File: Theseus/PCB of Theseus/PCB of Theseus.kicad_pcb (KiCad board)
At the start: 2 copper layers, 125 x 70 mm, 94 parts, among them J1 Screw_Terminal_01x04, J10 Screw_Terminal_01x03, J2 Screw_Terminal_01x04, J3 Screw_Terminal_01x03, J4 Screw_Terminal_01x06, J5 Programmer, J6 Micro_SD_Card, J7 Screw_Terminal_01x02, J8 Screw_Terminal_01x06, J9 Screw_Terminal_01x03, Q1 NMOS, Q2 NMOS, U1 TPS564257DRL, U10 INA326, U2 MCP2562, U3 REF200, U4 INA326, U5 INA326, U6 STM32H750VBTx, U7 REF200, U8 MX25L25645G, U9 REF200

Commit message: Theseus_Dev_Rev2
It's still the same PCB
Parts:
- removed H1, H2, H3, H4: ~, MountingHole:MountingHole_3.2mm_M3_Pad_Via
- removed J10, J9: Screw_Terminal_01x03, TerminalBlock_CUI:TerminalBlock_CUI_TB007-508-03_1x03_P5.08mm_Horizontal
- removed R10: 10k, Resistor_SMD:R_0402_1005Metric_Pad0.72x0.64mm_HandSolder
- removed R48, R49: 3.4k, Resistor_SMD:R_0402_1005Metric_Pad0.72x0.64mm_HandSolder
- removed R8: 221k, Resistor_SMD:R_0603_1608Metric_Pad0.98x0.95mm_HandSolder
- removed R9: 30k, Resistor_SMD:R_0603_1608Metric_Pad0.98x0.95mm_HandSolder
- removed U10, U5: INA326, Package_SO:MSOP-8_3x3mm_P0.65mm
- removed U7, U9: REF200, Package_SO:SOIC-8_3.9x4.9mm_P1.27mm
- added C25: 10u, Capacitor_SMD:C_0805_2012Metric_Pad1.18x1.45mm_HandSolder, F.Cu at (144.5, 86.1)
- added C26: 10u, Capacitor_SMD:C_0805_2012Metric_Pad1.18x1.45mm_HandSolder, B.Cu at (120.8, 79.4)
- added C27: 0.047u, Capacitor_SMD:C_0805_2012Metric_Pad1.18x1.45mm_HandSolder, F.Cu at (157.7, 78.1)
- added C28: 0.47u, Capacitor_SMD:C_0805_2012Metric_Pad1.18x1.45mm_HandSolder, F.Cu at (161.8, 78.1)
- added C29: 0.47u, Capacitor_SMD:C_0805_2012Metric_Pad1.18x1.45mm_HandSolder, F.Cu at (153.6, 78.1)
- added C30: 2n, Capacitor_SMD:C_0805_2012Metric_Pad1.18x1.45mm_HandSolder, F.Cu at (164.9, 62.3)
- added C31: 2n, Capacitor_SMD:C_0805_2012Metric_Pad1.18x1.45mm_HandSolder, F.Cu at (156.3, 62.3)
- added C32: 10u, Capacitor_SMD:C_0805_2012Metric_Pad1.18x1.45mm_HandSolder, F.Cu at (106.4, 54.5)
- added C33: 0.047u, Capacitor_SMD:C_0805_2012Metric_Pad1.18x1.45mm_HandSolder, F.Cu at (177.2, 80.8)
- added C34: 0.47u, Capacitor_SMD:C_0805_2012Metric_Pad1.18x1.45mm_HandSolder, F.Cu at (175.1, 77.2)
- added C35: 0.1u, Capacitor_SMD:C_0805_2012Metric_Pad1.18x1.45mm_HandSolder, F.Cu at (159.4, 40.1)
- added C36: 0.1u, Capacitor_SMD:C_0805_2012Metric_Pad1.18x1.45mm_HandSolder, F.Cu at (148.9, 66.6)
- added C37: 0.1u, Capacitor_SMD:C_0805_2012Metric_Pad1.18x1.45mm_HandSolder, F.Cu at (191.8, 84.8)
- added C38: 0.1u, Capacitor_SMD:C_0805_2012Metric_Pad1.18x1.45mm_HandSolder, F.Cu at (160.8, 65.2)
- added C39: 0.1u, Capacitor_SMD:C_0805_2012Metric_Pad1.18x1.45mm_HandSolder, F.Cu at (178.3, 70.7)
- added FB1: FerriteBead, Resistor_SMD:R_0805_2012Metric_Pad1.20x1.40mm_HandSolder, F.Cu at (150.5, 49.6)
- added H5: MountingHole, MountingHole:MountingHole_4.3mm_M4, F.Cu at (93.3, 33.7)
- added H6: MountingHole, MountingHole:MountingHole_4.3mm_M4, F.Cu at (93.3, 93.7)
- added H7: MountingHole, MountingHole:MountingHole_4.3mm_M4, F.Cu at (208.3, 33.7)
- added H8: MountingHole, MountingHole:MountingHole_4.3mm_M4, F.Cu at (208.3, 93.7)
- added J11: TB002-500-02BE, TerminalBlock_CUI:TerminalBlock_CUI_TB007-508-02_1x02_P5.08mm_Horizontal, F.Cu at (154.6, 95.6)
- added J12: TB002-500-02BE, TerminalBlock_CUI:TerminalBlock_CUI_TB007-508-02_1x02_P5.08mm_Horizontal, F.Cu at (164.3, 31.2)
- added R29: 10M ±1%, Resistor_SMD:R_0805_2012Metric_Pad1.20x1.40mm_HandSolder, F.Cu at (160.6, 86.9)
- added R30: 1M ±0.1%, Resistor_SMD:R_0805_2012Metric_Pad1.20x1.40mm_HandSolder, F.Cu at (153.6, 87.1)
- added R31: 806R, Resistor_SMD:R_0805_2012Metric_Pad1.20x1.40mm_HandSolder, F.Cu at (159.5, 82.9)
- added R32: 806R, Resistor_SMD:R_0805_2012Metric_Pad1.20x1.40mm_HandSolder, F.Cu at (155.7, 82.9)
- added R33: 20k, Resistor_SMD:R_0805_2012Metric_Pad1.20x1.40mm_HandSolder, F.Cu at (158.7, 71.2)
- added R34: 80.6k, Resistor_SMD:R_0805_2012Metric_Pad1.20x1.40mm_HandSolder, F.Cu at (165.0, 65.8)
- added R35: 20k, Resistor_SMD:R_0805_2012Metric_Pad1.20x1.40mm_HandSolder, F.Cu at (150.1, 71.0)
- added R36: 80.6k, Resistor_SMD:R_0805_2012Metric_Pad1.20x1.40mm_HandSolder, F.Cu at (156.3, 65.9)
- added R37: 806R, Resistor_SMD:R_0805_2012Metric_Pad1.20x1.40mm_HandSolder, F.Cu at (177.1, 84.1)
- added R38: 8.06k, Resistor_SMD:R_0805_2012Metric_Pad1.20x1.40mm_HandSolder, F.Cu at (179.5, 75.4)
- added TH1: PTS060301B100RP100, Resistor_SMD:R_0603_1608Metric_Pad0.98x0.95mm_HandSolder, F.Cu at (188.2, 99.1)
- added TP10: TestPoint, TestPoint:TestPoint_Pad_D2.0mm, F.Cu at (91.0, 61.6)
- added TP2: TC2+, TestPoint:TestPoint_Pad_D2.0mm, F.Cu at (163.2, 83.0)
- added TP3: TC2-, TestPoint:TestPoint_Pad_D2.0mm, F.Cu at (151.9, 83.0)
- added TP4: TC1+, TestPoint:TestPoint_Pad_D2.0mm, F.Cu at (175.3, 31.5)
- added TP5: TC1-, TestPoint:TestPoint_Pad_D2.0mm, F.Cu at (158.8, 31.3)
- added TP6: TC3+, TestPoint:TestPoint_Pad_D2.0mm, F.Cu at (188.1, 85.9)
- added TP7: TC3-, TestPoint:TestPoint_Pad_D2.0mm, F.Cu at (173.1, 85.8)
- added TP8: RTD1, TestPoint:TestPoint_Pad_D2.0mm, F.Cu at (193.1, 98.1)
- added TP9: RTD2, TestPoint:TestPoint_Pad_D2.0mm, F.Cu at (196.9, 98.1)
- added U11: INA326, Package_SO:MSOP-8_3x3mm_P0.65mm, F.Cu at (163.0, 71.0)
- added U12: INA326, Package_SO:MSOP-8_3x3mm_P0.65mm, F.Cu at (154.3, 71.1)
- added U13: MAX6675, Package_SO:SOIC-8_3.9x4.9mm_P1.27mm, F.Cu at (166.8, 42.6)
- C1: value 100nF -> 10u; footprint Capacitor_SMD:C_0603_1608Metric_Pad1.08x0.95mm_HandSolder -> Capacitor_SMD:C_0805_2012Metric_Pad1.18x1.45mm_HandSolder
- C10, C11, C12, C13, C14, C15, C16, C22, C6, C7, C9: footprint Capacitor_SMD:C_0603_1608Metric_Pad1.08x0.95mm_HandSolder -> Capacitor_SMD:C_0805_2012Metric_Pad1.18x1.45mm_HandSolder
- C17: value 1u -> 1n; footprint Capacitor_SMD:C_0402_1005Metric_Pad0.74x0.62mm_HandSolder -> Capacitor_SMD:C_0805_2012Metric_Pad1.18x1.45mm_HandSolder
- C18, C19: value 0.1uF -> 0.1u; footprint Capacitor_SMD:C_0201_0603Metric_Pad0.64x0.40mm_HandSolder -> Capacitor_SMD:C_0805_2012Metric_Pad1.18x1.45mm_HandSolder
- C2: value 22uF -> 100n
- C20, C21: value 510pF -> 0.5n; footprint Capacitor_SMD:C_0201_0603Metric_Pad0.64x0.40mm_HandSolder -> Capacitor_SMD:C_0805_2012Metric_Pad1.18x1.45mm_HandSolder
- C23: value 510pF -> 0.47u; footprint Capacitor_SMD:C_0201_0603Metric_Pad0.64x0.40mm_HandSolder -> Capacitor_SMD:C_0805_2012Metric_Pad1.18x1.45mm_HandSolder
- C24, C4: value 22uF -> 22u
- C3: value 10pF -> 100n; footprint Capacitor_SMD:C_0402_1005Metric_Pad0.74x0.62mm_HandSolder -> Capacitor_SMD:C_0805_2012Metric_Pad1.18x1.45mm_HandSolder
- C5: value 100nF -> 22u; footprint Capacitor_SMD:C_0603_1608Metric_Pad1.08x0.95mm_HandSolder -> Capacitor_SMD:C_0805_2012Metric_Pad1.18x1.45mm_HandSolder
- C8: footprint Capacitor_SMD:C_0603_1608Metric_Pad1.08x0.95mm_HandSolder -> Capacitor_SMD:C_0805_2012Metric_Pad1.18x1.45mm_HandSolder; moved to B.Cu
- D1, D5: value D -> 1N4150-W-E3-18; footprint Diode_SMD:D_SMB-SMC_Universal_Handsoldering -> Diode_SMD:D_SOD-123
- F1: value TBD -> 3.5A 0685T3500-01
- J1, J2: value Screw_Terminal_01x04 -> TB001-500-04BE
- J3: value Screw_Terminal_01x03 -> TB002-500-02BE; footprint TerminalBlock_CUI:TerminalBlock_CUI_TB007-508-03_1x03_P5.08mm_Horizontal -> TerminalBlock_CUI:TerminalBlock_CUI_TB007-508-02_1x02_P5.08mm_Horizontal
- J4, J8: value Screw_Terminal_01x06 -> TB003-500-P06BE
- J5: value Programmer -> Programmer GRPB022VWQS-RC
- J6: value Micro_SD_Card -> Micro SD Holder 0472192001
- J7: value Screw_Terminal_01x02 -> TB002-500-02BE
- L1: value 3.3uH -> 2.2u; footprint Fydp_footprints:VLS6045EX-3R3N -> Fydp_footprints:SPM6530T-2R2M
- Q1, Q2: value NMOS -> NX3020NAK,215
- R1, R2, R3: value 150R -> 150R ±0.1%; footprint Resistor_SMD:R_0603_1608Metric_Pad0.98x0.95mm_HandSolder -> Resistor_SMD:R_0805_2012Metric_Pad1.20x1.40mm_HandSolder
- R11: value 45.3k -> 33.2k; footprint Resistor_SMD:R_0603_1608Metric_Pad0.98x0.95mm_HandSolder -> Resistor_SMD:R_0805_2012Metric_Pad1.20x1.40mm_HandSolder
- R12: value 10k -> 10.2k; footprint Resistor_SMD:R_0402_1005Metric_Pad0.72x0.64mm_HandSolder -> Resistor_SMD:R_0805_2012Metric_Pad1.20x1.40mm_HandSolder
- R13, R14, R15, R16, R17: footprint Resistor_SMD:R_0402_1005Metric_Pad0.72x0.64mm_HandSolder -> Resistor_SMD:R_0805_2012Metric_Pad1.20x1.40mm_HandSolder; moved to B.Cu
- R18, R19: value 2k -> 32.4k ±0.1%; footprint Resistor_SMD:R_0603_1608Metric_Pad0.98x0.95mm_HandSolder -> Resistor_SMD:R_0805_2012Metric_Pad1.20x1.40mm_HandSolder
- R20: value 76.8R -> 100R ±0.1%; footprint Resistor_SMD:R_0603_1608Metric_Pad0.98x0.95mm_HandSolder -> Resistor_SMD:R_0805_2012Metric_Pad1.20x1.40mm_HandSolder
- R21: value 324k -> 8.06k; footprint Resistor_SMD:R_0201_0603Metric_Pad0.64x0.40mm_HandSolder -> Resistor_SMD:R_0805_2012Metric_Pad1.20x1.40mm_HandSolder
- R22: value 76.8R -> 200k; footprint Resistor_SMD:R_0603_1608Metric_Pad0.98x0.95mm_HandSolder -> Resistor_SMD:R_0805_2012Metric_Pad1.20x1.40mm_HandSolder
- R23: value 2k -> 200k; footprint Resistor_SMD:R_0603_1608Metric_Pad0.98x0.95mm_HandSolder -> Resistor_SMD:R_0805_2012Metric_Pad1.20x1.40mm_HandSolder
- R24, R25: value 324k -> 1M ±0.1%; footprint Resistor_SMD:R_0201_0603Metric_Pad0.64x0.40mm_HandSolder -> Resistor_SMD:R_0805_2012Metric_Pad1.20x1.40mm_HandSolder
- R26: value 76.8R -> 806R; footprint Resistor_SMD:R_0603_1608Metric_Pad0.98x0.95mm_HandSolder -> Resistor_SMD:R_0805_2012Metric_Pad1.20x1.40mm_HandSolder
- R27, R28: footprint Resistor_SMD:R_0402_1005Metric_Pad0.72x0.64mm_HandSolder -> Resistor_SMD:R_0805_2012Metric_Pad1.20x1.40mm_HandSolder
- R4, R44, R45, R5, R6, R7: footprint Resistor_SMD:R_0603_1608Metric_Pad0.98x0.95mm_HandSolder -> Resistor_SMD:R_0805_2012Metric_Pad1.20x1.40mm_HandSolder
- R46: value 30K -> 3M ±1%; footprint Resistor_SMD:R_0603_1608Metric_Pad0.98x0.95mm_HandSolder -> Resistor_SMD:R_0805_2012Metric_Pad1.20x1.40mm_HandSolder
- R47: value 10K -> 1M ±0.1%; footprint Resistor_SMD:R_0402_1005Metric_Pad0.72x0.64mm_HandSolder -> Resistor_SMD:R_0805_2012Metric_Pad1.20x1.40mm_HandSolder
- U1: value TPS564257DRL -> TPS565201DDC; footprint Package_TO_SOT_SMD:SOT-563 -> Package_TO_SOT_SMD:SOT-23-6_Handsoldering
- U3: value REF200 -> INA326; footprint Package_SO:SOIC-8_3.9x4.9mm_P1.27mm -> Package_SO:MSOP-8_3x3mm_P0.65mm
- U8: footprint Package_SO:SOIC-16W_7.5x10.3mm_P1.27mm -> Package_SO:SOIC-8_5.3x5.3mm_P1.27mm
- moved D3 86.4 mm to (186.8, 50.1), turned to 180 degrees
- moved D4 85.8 mm to (198.2, 50.4), turned to 180 degrees
- moved R27 85.7 mm to (183.1, 42.1)
- moved R28 85.5 mm to (194.4, 42.0)
- moved D1 84.6 mm to (186.0, 40.0)
- moved Q1 84.4 mm to (186.8, 43.3), turned to -90 degrees
- moved D5 84.4 mm to (197.2, 39.8)
- moved Q2 84.2 mm to (198.1, 43.1), turned to -90 degrees
- moved R4 83.6 mm to (183.1, 50.1), turned to 0 degrees
- moved J1 83.2 mm to (182.7, 31.3)
- moved R7 83.1 mm to (194.4, 50.4), turned to 0 degrees
- moved C17 82.8 mm to (158.2, 49.5)
- moved C15 81.2 mm to (150.8, 44.5), turned to 0 degrees
- moved R6 81.0 mm to (181.1, 45.5), turned to 180 degrees
- moved R5 80.8 mm to (192.4, 45.5), turned to 180 degrees
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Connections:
- net /MCU/RTD_1 renamed /MCU/TC3
- C20 pad 1: Net-(U5-R2) -> Net-(U3-R2)
- C21 pad 2: GND -> Net-(C21-Pad2)
- C23 pad 1: Net-(U10-R2) -> GND
- C23 pad 2: GND -> Net-(U4-+)
- C3 pad 1: +3.3V -> Net-(U1-SW)
- C3 pad 2: Net-(U1-FB) -> Net-(U1-VBST)
- R11 pad 2: Net-(U1-FB) -> Net-(U1-VFB)
- R12 pad 1: Net-(U1-FB) -> Net-(U1-VFB)
- R18 pad 1: Net-(R18-Pad1) -> +3.3V
- R18 pad 2: Net-(R18-Pad2) -> /Temperature Sensors/RTD+
- R19 pad 1: Net-(R19-Pad1) -> +3.3V
- R19 pad 2: Net-(R19-Pad2) -> Net-(U3--)
- R20 pad 1: Net-(U5--) -> Net-(U3--)
- R20 pad 2: Net-(J10-Pin_1) -> GND
- R21 pad 1: Net-(U5-R2) -> Net-(R21-Pad1)
- R21 pad 2: GND -> Net-(R21-Pad2)
- R22 pad 1: Net-(U3-I2_LOW) -> Net-(U3-R2)
- R22 pad 2: Net-(J3-Pin_1) -> GND
- R23 pad 1: Net-(R23-Pad1) -> Net-(U4-R2)
- R23 pad 2: Net-(R23-Pad2) -> Net-(C21-Pad2)
- R24 pad 1: Net-(U4-R2) -> +3.3V
- R24 pad 2: GND -> Net-(J3-Pin_2)
- R25 pad 1: Net-(U10-R2) -> Net-(J3-Pin_1)
- R26 pad 1: Net-(U10--) -> Net-(J3-Pin_2)
- R26 pad 2: Net-(J9-Pin_1) -> Net-(U4-+)
- U1 pad 1: +BATT -> GND
- U1 pad 2: Net-(U1-EN) -> Net-(U1-SW)
- U1 pad 3: Net-(U1-SW) -> +BATT
- U1 pad 4: Net-(U1-PG) -> Net-(U1-VFB)
- U1 pad 5: Net-(U1-FB) -> +BATT
- U1 pad 6: GND -> Net-(U1-VBST)
- U3 pad 1: Net-(J3-Pin_2) -> Net-(R21-Pad1)
- U3 pad 2: Net-(U3-I2_LOW) -> Net-(U3--)
- U3 pad 3: unconnected-(U3-MIRROR_COMMON-Pad3) -> /Temperature Sensors/RTD+
- U3 pad 4: unconnected-(U3-MIRROR_OUTPUT-Pad4) -> GND
- U3 pad 5: unconnected-(U3-MIRROR_INPUT-Pad5) -> Net-(U3-R2)
- U3 pad 6: unconnected-(U3-SUBSTRATE-Pad6) -> Net-(C21-Pad2)
- U3 pad 8: +3.3V -> Net-(R21-Pad2)
- U4 pad 1: Net-(R19-Pad1) -> Net-(R38-Pad1)
- U4 pad 2: Net-(U3-I2_LOW) -> Net-(U4--)
- U4 pad 3: Net-(J3-Pin_2) -> Net-(U4-+)
- U4 pad 8: Net-(R19-Pad2) -> Net-(R38-Pad2)
- U6 pad 1: /MCU/RTD_3 -> /MCU/TC2+
- U6 pad 2: /MCU/RTD_2 -> /MCU/TC2-
- U6 pad 21: +3.3V -> Net-(U6-VDDA)
- U6 pad 28: /MCU/LED_BLUE -> /MCU/TC1_NSS
- U6 pad 29: /MCU/LED_RED -> /MCU/TC1_SCK
- U6 pad 33: unconnected-(U6-PC5-Pad33) -> /MCU/TC1_SI
- U6 pad 56: unconnected-(U6-PD9-Pad56) -> /MCU/LED_RED
- U6 pad 57: unconnected-(U6-PD10-Pad57) -> /MCU/LED_BLUE
- U8 pad 1: unconnected-(U8-NC/SOIC3-Pad1) -> /MCU/SPI_NSS
- U8 pad 2: +3.3V -> /MCU/SPI_MISO
- U8 pad 3: /MCU/MEM_~{RESET} -> unconnected-(U8-WP#/SIO2-Pad3)
- U8 pad 4: unconnected-(U8-NC-Pad4) -> GND
- U8 pad 5: unconnected-(U8-NC-Pad5) -> /MCU/SPI_MOSI
- U8 pad 6: unconnected-(U8-NC-Pad6) -> /MCU/SPI_SCK
- U8 pad 7: /MCU/SPI_NSS -> /MCU/MEM_~{RESET}
- U8 pad 8: /MCU/SPI_MISO -> +3.3V
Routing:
- net GND: track 141.8 -> 208.8 mm, vias 5 -> 23
- net +3.3V: track 85.2 -> 137.4 mm
- net +BATT: track 96.0 -> 146.3 mm
- net /MCU/RTD_2: track 40.1 -> 0.00 mm
- net /CAN_Rx: track 66.2 -> 27.1 mm
- net /MCU/VALVE_2: track 23.6 -> 60.7 mm
- net /CAN_Tx: track 58.6 -> 22.6 mm
- net /MCU/VALVE_1: track 13.2 -> 44.6 mm
- net /MCU/SD_CLK: track 58.5 -> 28.9 mm
- net /MCU/TC1_SI: track 0.00 -> 29.3 mm
- net /MCU/SD_D0: track 75.2 -> 47.3 mm, vias 0 -> 1
- net /MCU/SPI_MISO: track 36.7 -> 9.02 mm
- net /MCU/PT_1: track 50.3 -> 22.9 mm
- net /MCU/TC1_NSS: track 0.00 -> 25.6 mm
- net /MCU/PT_2: track 40.5 -> 15.3 mm
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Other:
- board size 125 x 70 mm -> 135 x 80 mm
- board text added: "BATT"
- board text added: "CAN"
- board text added: "HALL"
- board text added: "MATTHEW GORDON"
- board text added: "PCB OF THESEUS DEV EDITION, REV 2"
- board text added: "PT"
- board text added: "TC1"
- board text added: "TC2"
- board text added: "TC3"
- board text removed: "+12V"
- board text removed: "+3.3V"
- board text removed: "5V"
- board text removed: "CANH"
- board text removed: "CANL"
- board text removed: "GND"
- board text removed: "HALL SENSORS"
- board text removed: "IF YOU'RE READING THIS, YOU'RE HOLDING THE PCB UPSIDE DOWN"
- board text removed: "PTS"
- board text removed: "RTD"
- board text removed: "SENSE"
- board text removed: "THE PCB OF THESEUS REV. 1.0 MATTHEW GORDON"

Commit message: Minor routing changes
Still the same PCB
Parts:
- added G***: LOGO, Tutorial_Footprints:Logo_Horizontal_Silkscreen_10mm, B.Cu at (147.3, 66.4)
- moved C13 23.0 mm to (158.9, 52.9), turned to 0 degrees
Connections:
- U6 pad 30: unconnected-(U6-PA6-Pad30) -> /MCU/TC1_SI
- U6 pad 33: /MCU/TC1_SI -> unconnected-(U6-PC5-Pad33)
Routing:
- net +3.3V: track 137.4 -> 140.0 mm
- net /MCU/TC1_SI: track 29.3 -> 28.0 mm
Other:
- board text added: "IF YOU'RE READING THIS THE PCB IS UPSIDE-DOWN (OR YOU'RE IN THE SHADOW REALM)"

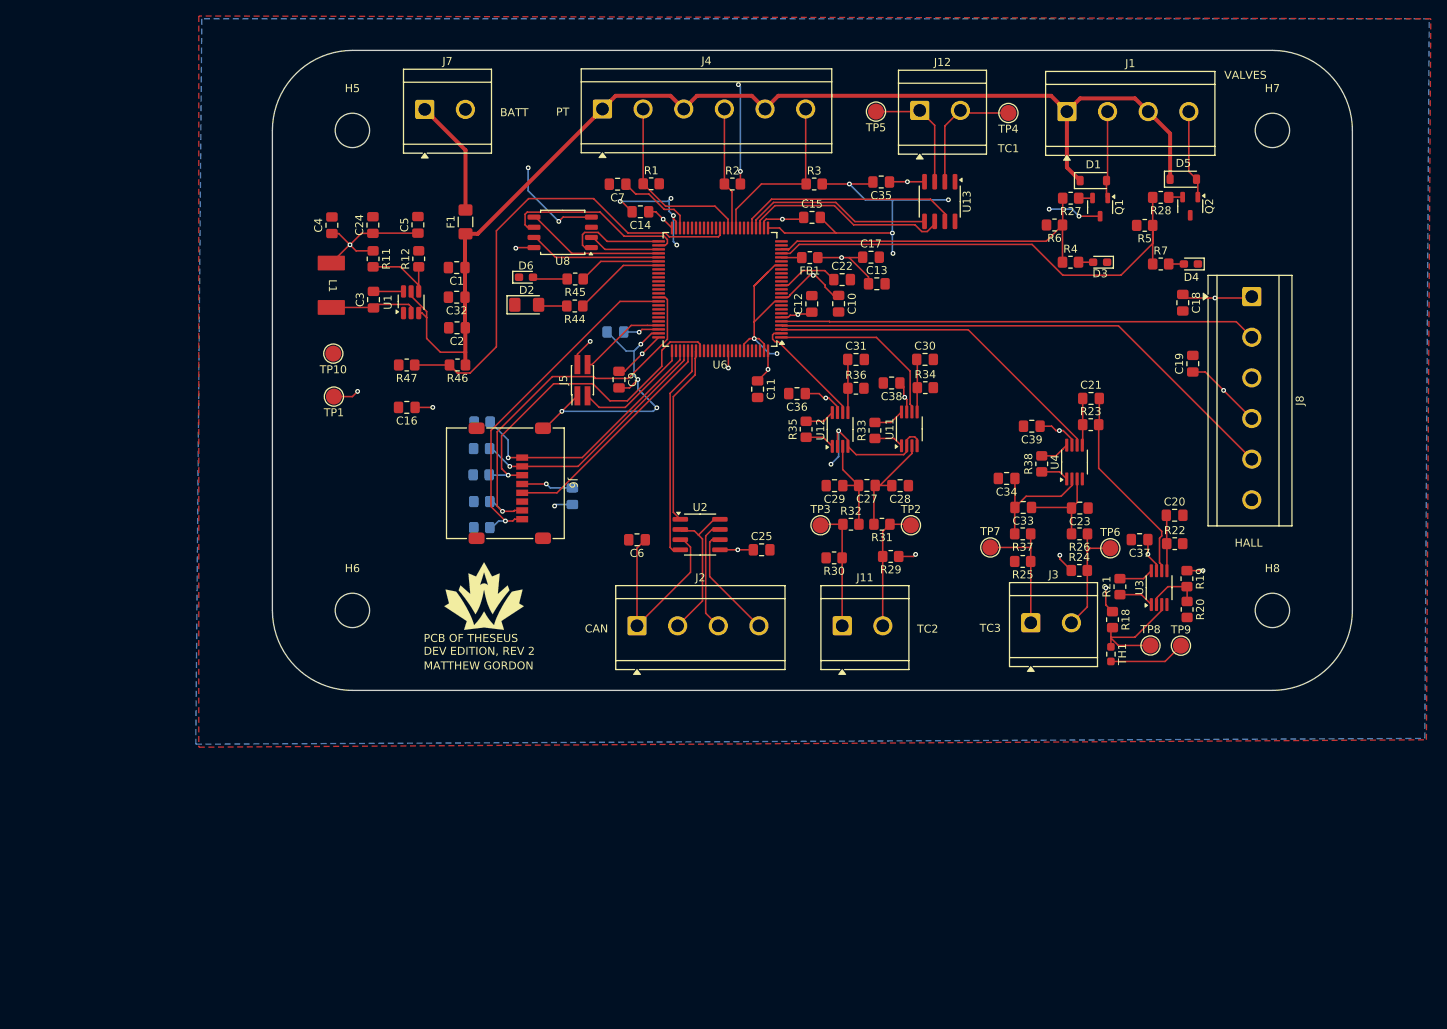
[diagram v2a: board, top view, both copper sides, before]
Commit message: Fixes V3
- Copied Ferrite Bead P/N from processor
- Added external oscillator
- Made status LED pins pull-down
- Copied processor programming header
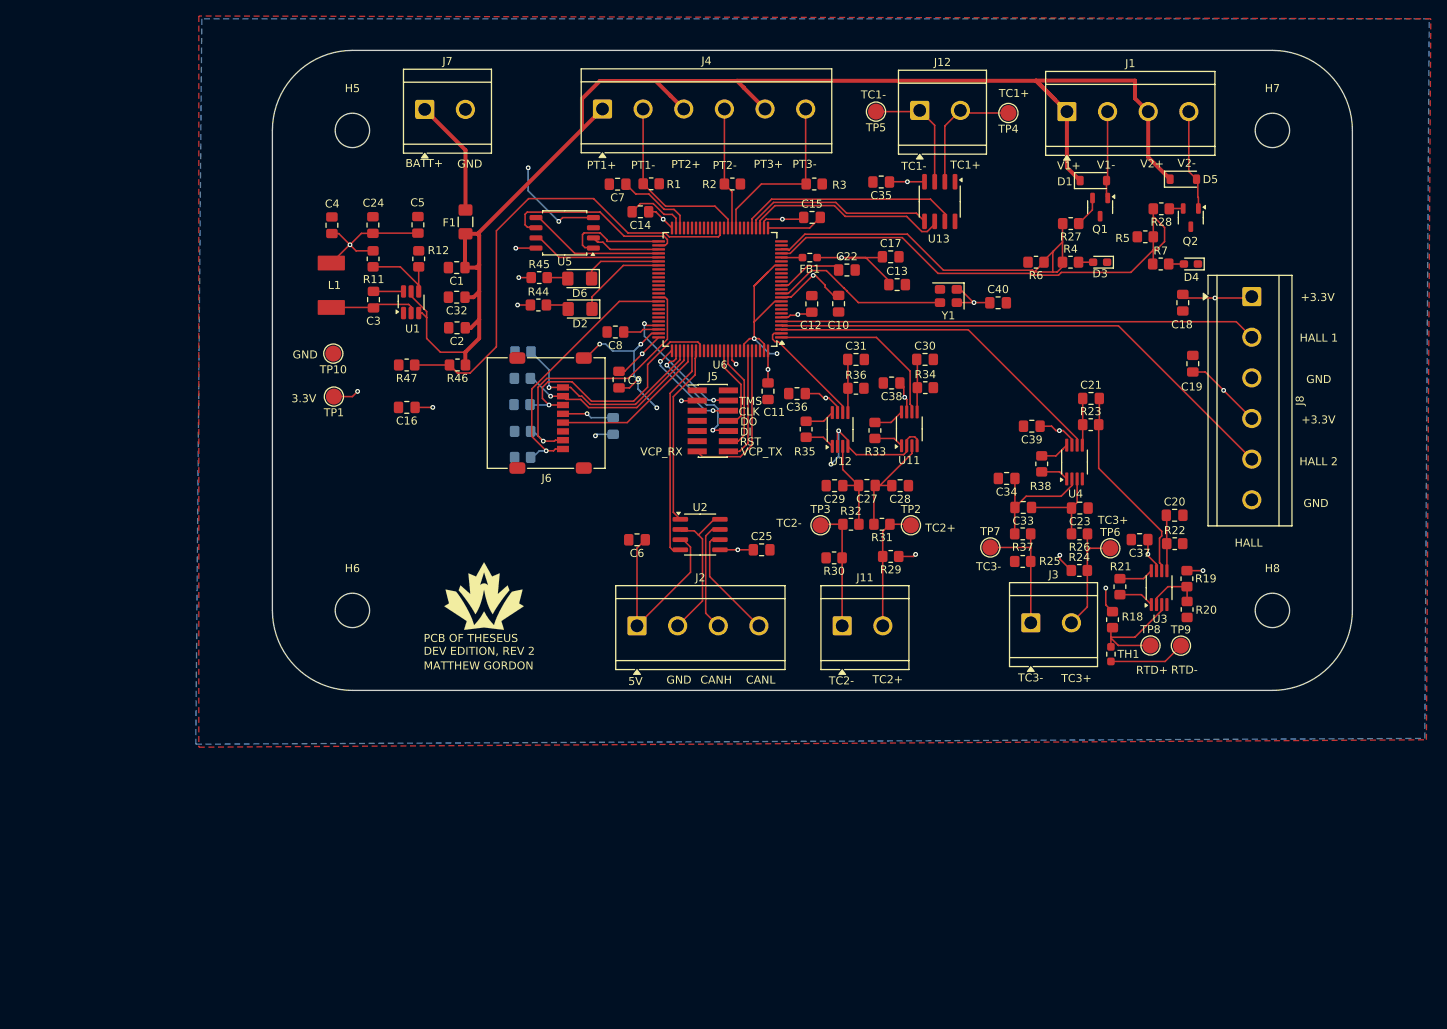
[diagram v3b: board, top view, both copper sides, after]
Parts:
- removed U8: MX25L25645G, Package_SO:SOIC-8_5.3x5.3mm_P1.27mm
- added C40: 0.01uF, Capacitor_SMD:C_0805_2012Metric_Pad1.18x1.45mm_HandSolder, F.Cu at (174.1, 55.2)
- added U5: MX25L25645G, Package_SO:SOIC-8_5.3x5.3mm_P1.27mm, F.Cu at (119.9, 46.5)
- added Y1: ASE-4.000MHz-L-C-T, Oscillator:Oscillator_SMD_Abracon_ASE-4Pin_3.2x2.5mm, F.Cu at (167.8, 54.4)
- C8: moved to F.Cu
- D6: footprint Diode_SMD:D_0603_1608Metric_Pad1.05x0.95mm_HandSolder -> Diode_SMD:D_1206_3216Metric_Pad1.42x1.75mm_HandSolder
- FB1: value FerriteBead -> PE-0603PFB121ST; footprint Resistor_SMD:R_0805_2012Metric_Pad1.20x1.40mm_HandSolder -> Resistor_SMD:R_0603_1608Metric_Pad0.98x0.95mm_HandSolder
- J5: value Programmer GRPB022VWQS-RC -> CN4 STDC14 (Programmer); footprint Connector_PinHeader_1.27mm:PinHeader_2x02_P1.27mm_Vertical_SMD -> Connector_PinHeader_1.27mm:PinHeader_2x07_P1.27mm_Vertical_SMD
- moved J5 17.1 mm to (138.4, 70.0), turned to 0 degrees
- moved C26 10.1 mm to (126.0, 70.6)
- moved J6 10.1 mm to (117.6, 69.0)
- moved R14 10.1 mm to (114.6, 64.7)
- moved R16 10.1 mm to (114.6, 71.3)
- moved R17 10.1 mm to (114.6, 74.5)
- moved R13 10.1 mm to (114.7, 61.4)
- moved R15 10.1 mm to (114.5, 68.0)
- moved D6 6.71 mm to (121.8, 52.2), turned to 180 degrees
- moved D2 6.70 mm to (121.8, 56.0), turned to 180 degrees
- moved R6 5.19 mm to (178.8, 50.1)
- moved R44 4.55 mm to (116.6, 55.5), turned to 0 degrees
- moved R45 4.50 mm to (116.7, 52.1), turned to 0 degrees
- moved R27 3.18 mm to (183.1, 45.3)
- moved C13 2.54 mm to (161.4, 53.0)
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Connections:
- net /MCU/SWDIO renamed /MCU/TMS
- D2 pad 1: GND -> /MCU/LED_BLUE
- D6 pad 1: GND -> /MCU/LED_RED
- J5 pad 1: GND -> unconnected-(J5-Pin_1-Pad1)
- J5 pad 2: +3.3V -> unconnected-(J5-Pin_2-Pad2)
- J5 pad 3: /MCU/SWCLK -> +3.3V
- R44 pad 1: /MCU/LED_BLUE -> +3.3V
- R45 pad 1: /MCU/LED_RED -> +3.3V
- U6 pad 12: unconnected-(U6-PH0-Pad12) -> /MCU/OSC_IN
- U6 pad 76: /MCU/SWCLK -> /MCU/TCK
- U6 pad 77: unconnected-(U6-PA15-Pad77) -> /MCU/TDI
- U6 pad 89: unconnected-(U6-PB3-Pad89) -> /MCU/TDO
- U6 pad 90: +3.3V -> /MCU/TRST
- U6 pad 91: unconnected-(U6-PB5-Pad91) -> +3.3V
- U6 pad 95: unconnected-(U6-PB8-Pad95) -> /MCU/VCP_TX
- U6 pad 96: unconnected-(U6-PB9-Pad96) -> /MCU/VCP_RX
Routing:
- net GND: track 208.8 -> 128.5 mm, vias 23 -> 11
- net +BATT: track 146.3 -> 180.9 mm
- net /MCU/OSC_IN: track 0.00 -> 22.7 mm
- net /MCU/VCP_RX: track 0.00 -> 19.5 mm
- net /MCU/TDI: track 0.00 -> 16.2 mm, vias 0 -> 2
- net /MCU/SWCLK: track 14.8 -> 0.00 mm
- net /MCU/VCP_TX: track 0.00 -> 14.4 mm
- net /MCU/TRST: track 0.00 -> 13.7 mm
- net /MCU/TCK: track 0.00 -> 13.4 mm, vias 0 -> 2
- net +3.3V: track 140.0 -> 152.3 mm, vias 26 -> 29
- net /MCU/TDO: track 0.00 -> 10.8 mm
- net /MCU/SD_D1: track 44.2 -> 33.3 mm
- net /MCU/SD_D0: track 47.3 -> 36.5 mm
- net /MCU/SD_CMD: track 42.9 -> 33.3 mm
- net /MCU/SD_CLK: track 28.9 -> 20.2 mm
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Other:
- board text added: "+3.3V"
- board text added: "3.3V"
- board text added: "5V"
- board text added: "BATT+"
- board text added: "CANH"
- board text added: "CANL"
- board text added: "CLK"
- board text added: "DI"
- board text added: "DO"
- board text added: "GND"
- board text added: "HALL 1"
- board text added: "HALL 2"
- board text added: "PT1+"
- board text added: "PT1-"
- board text added: "PT2+"
- board text added: "PT2-"
- board text added: "PT3+"
- board text added: "PT3-"
- board text added: "RST"
- board text added: "RTD+"
- board text added: "RTD-"
- board text added: "TC1+"
- board text added: "TC1-"
- board text added: "TC2+"
- board text added: "TC2-"
- board text added: "TC3+"
- board text added: "TC3-"
- board text added: "TMS"
- board text added: "V1+"
- board text added: "V1-"
- board text added: "V2+"
- board text added: "V2-"
- board text added: "VCP_RX"
- board text added: "VCP_TX"
- board text removed: "BATT"
- board text removed: "CAN"
- board text removed: "PT"
- board text removed: "TC1"
- board text removed: "TC2"
- board text removed: "TC3"
- board text removed: "VALVES"

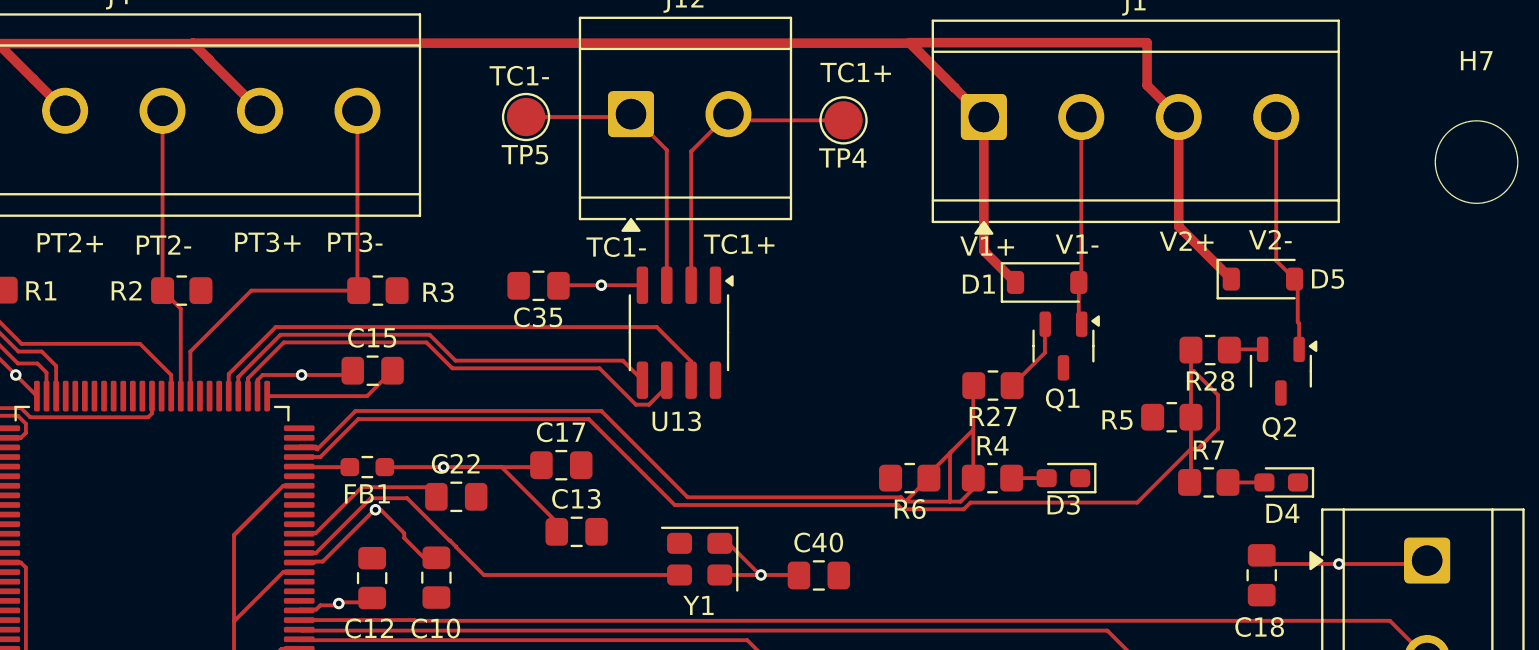
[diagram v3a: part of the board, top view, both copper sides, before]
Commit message: NMOS and Diode Update
Updated Diode and NMOS to support 1A max. Fixed valve state LED to draw from BATT instead of MCU.
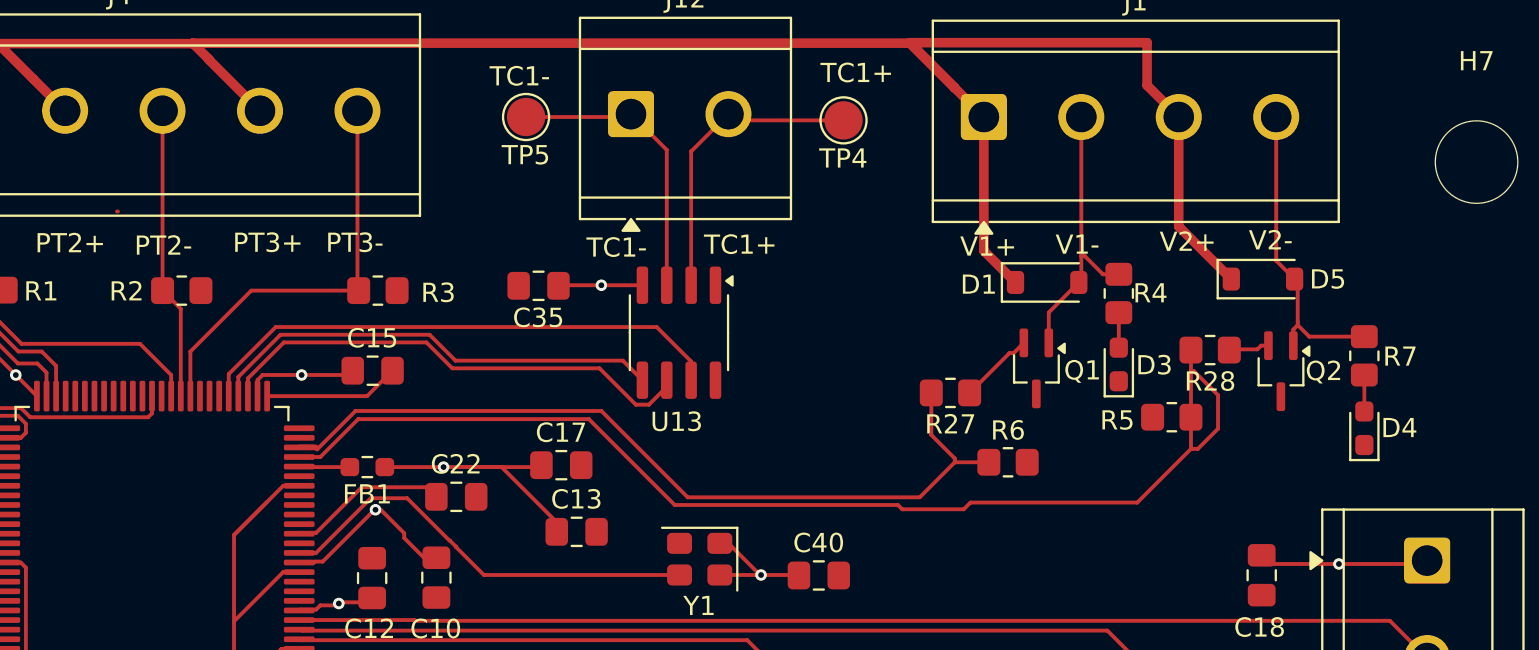
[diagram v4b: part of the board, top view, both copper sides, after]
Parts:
- D1, D5: value 1N4150-W-E3-18 -> CDBW140-G
- Q1, Q2: value NX3020NAK,215 -> DMG1012UW-7; footprint Package_TO_SOT_SMD:SOT-23-3 -> Package_TO_SOT_SMD:SOT-323_SC-70_Handsoldering
- R4, R7: value 169R -> 649R
- moved R4 11.7 mm to (189.7, 40.5), turned to -90 degrees
- moved R7 10.5 mm to (202.5, 43.8), turned to -90 degrees
- moved D3 6.59 mm to (189.7, 44.2), turned to 90 degrees
- moved R6 5.19 mm to (183.9, 49.3), turned to 0 degrees
- moved D4 5.17 mm to (202.5, 47.5), turned to 90 degrees
- moved R27 2.25 mm to (180.9, 45.7)
- moved Q1 1.83 mm to (185.4, 44.4)
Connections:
- R4 pad 1: /MCU/VALVE_1 -> Net-(D1-A)
- R7 pad 1: /MCU/VALVE_2 -> Net-(D5-A)
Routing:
- net /MCU/VALVE_1: track 51.6 -> 43.7 mm
- net Net-(D1-A): track 10.9 -> 14.8 mm
- net Net-(D5-A): track 12.6 -> 16.2 mm
- net /MCU/VALVE_2: track 63.0 -> 61.2 mm
